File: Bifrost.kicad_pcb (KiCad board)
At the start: 4 copper layers, 68.6 x 53.3 mm, 109 parts, among them IC1 DS1085Z-10+, IC2 DS1085Z-10+, J1 OIP, J10 Barrel_Jack_Switch, J5 CalCK, U1 HMC900LP5E, U2 HMC860LP3E, U5 74AHC1G04, U6 74AHC1G04

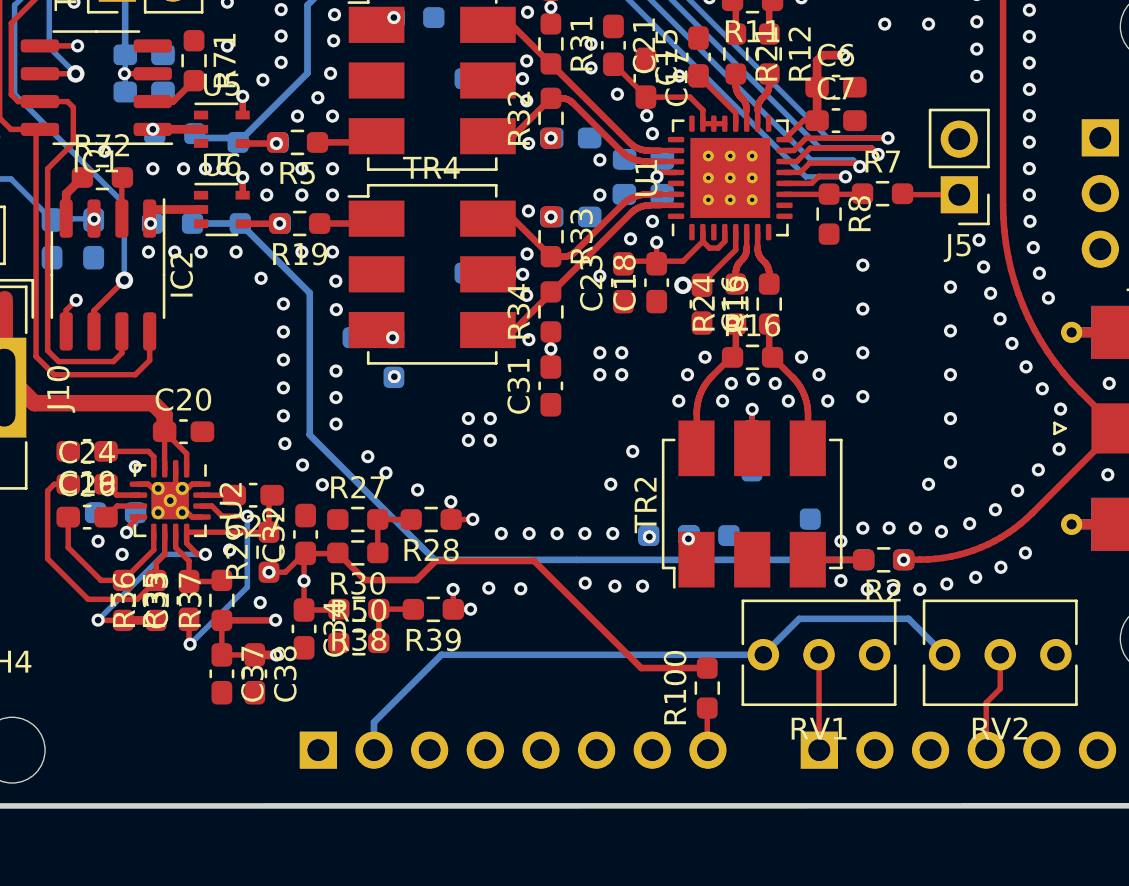
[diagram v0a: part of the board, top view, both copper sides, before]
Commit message: Added capacitors on potars
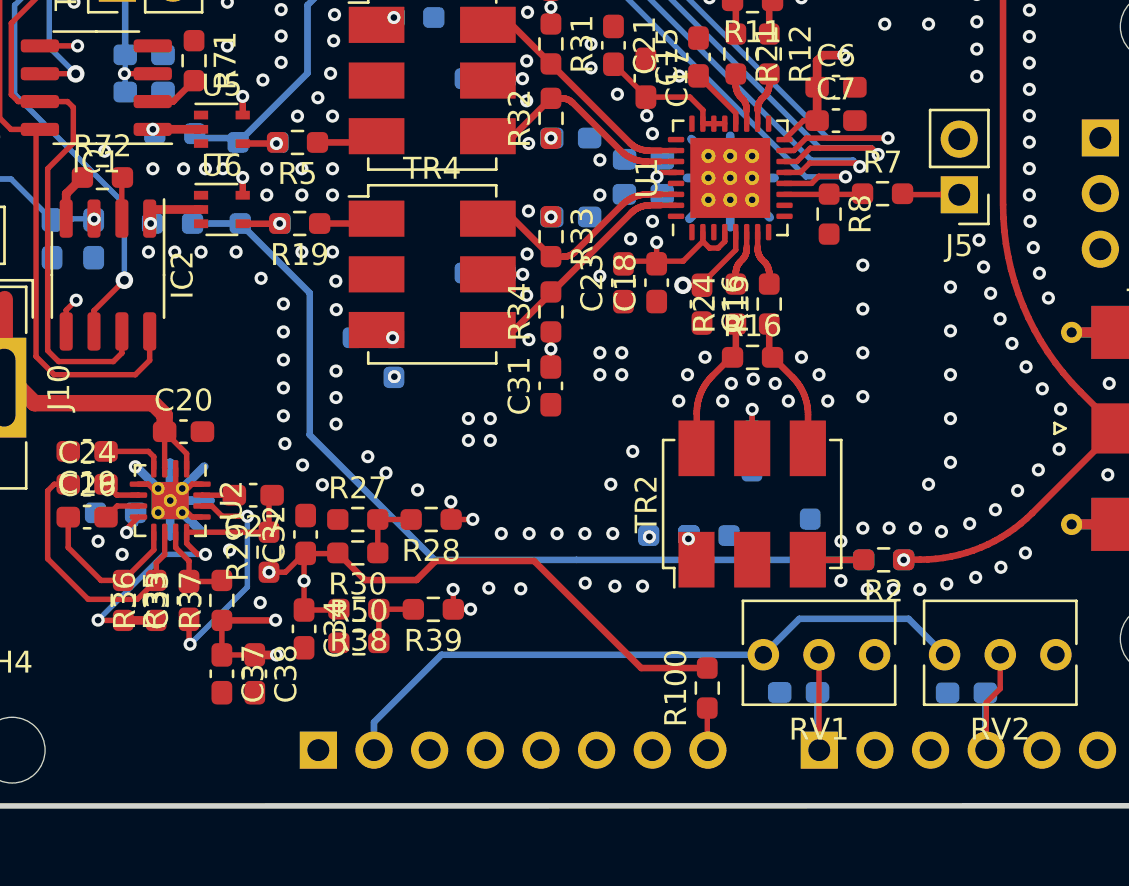
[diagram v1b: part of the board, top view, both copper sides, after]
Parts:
- added C5: 100n, Capacitor_SMD:C_0603_1608Metric_Pad1.08x0.95mm_HandSolder, B.Cu at (164.1, 126.5)
- added C8: 100n, Capacitor_SMD:C_0603_1608Metric_Pad1.08x0.95mm_HandSolder, B.Cu at (171.7, 126.5)
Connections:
- AD1 pad 2: (no net) -> /AD1
- AD1 pad 3: (no net) -> /AD2
- AD1 pad 5: (no net) -> /AD4
- AD1 pad 6: (no net) -> /AD5
- ICSP1 pad 1: (no net) -> /MISO2
- ICSP1 pad 2: (no net) -> /+5V_Adr_3
- ICSP1 pad 3: (no net) -> /SCK2
- ICSP1 pad 4: (no net) -> /MOSI2
- ICSP1 pad 5: (no net) -> /RESET2
- ICSP2 pad 1: (no net) -> /MISO_0
- ICSP2 pad 2: (no net) -> /+5V_Ard_0
- ICSP2 pad 3: (no net) -> /SCK_0
- ICSP2 pad 4: (no net) -> /MOSI_0
- ICSP2 pad 5: (no net) -> /RESET_0
- IOH1 pad 1: (no net) -> /IO8
- IOH1 pad 2: (no net) -> /IO9
- IOH1 pad 8: (no net) -> /AREF
- IOL1 pad 1: (no net) -> /IO0
- IOL1 pad 2: (no net) -> /IO1
- IOL1 pad 3: (no net) -> /IO2
- IOL1 pad 4: (no net) -> /IO3
- IOL1 pad 5: (no net) -> /IO4
- IOL1 pad 6: (no net) -> /IO5
- POWER1 pad 1: (no net) -> Net-(POWER1-Pad1)
- POWER1 pad 3: (no net) -> /RESET
- POWER1 pad 4: (no net) -> /+3V3
- POWER1 pad 5: (no net) -> /+5V_Ard_1
- TR1 pad 2: (no net) -> Net-(TR1-Pad2)
- TR2 pad 2: (no net) -> Net-(TR2-Pad2)
- TR3 pad 2: (no net) -> Net-(TR3-Pad2)
- TR4 pad 2: (no net) -> Net-(TR4-Pad2)
- U1 pad 1: (no net) -> Net-(U1-Pad1)
- U1 pad 10: (no net) -> Net-(U1-Pad10)
- U1 pad 17: (no net) -> Net-(U1-Pad17)
- U1 pad 24: (no net) -> Net-(U1-Pad24)
- U1 pad 25: (no net) -> Net-(U1-Pad25)
- U1 pad 29: (no net) -> Net-(U1-Pad29)
- U1 pad 3: (no net) -> Net-(U1-Pad3)
- U1 pad 32: (no net) -> Net-(U1-Pad32)
- U1 pad 8: (no net) -> Net-(U1-Pad8)
- U1 pad 9: (no net) -> Net-(U1-Pad9)
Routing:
- net GND: track 8.77 -> 42.4 mm
- net /AD0: track 4.36 -> 7.02 mm
- net /AD3: track 4.62 -> 7.25 mm

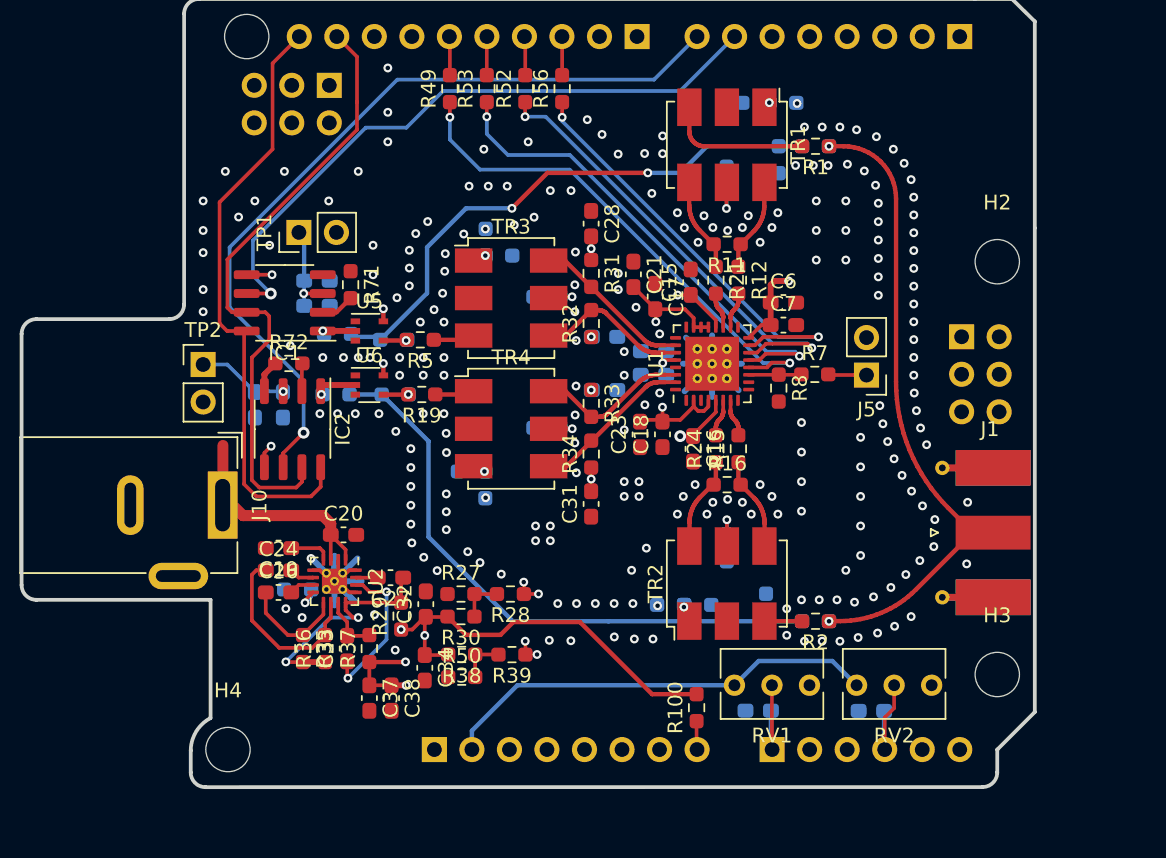
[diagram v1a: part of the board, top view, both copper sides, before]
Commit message: Rearranged the serigraphs
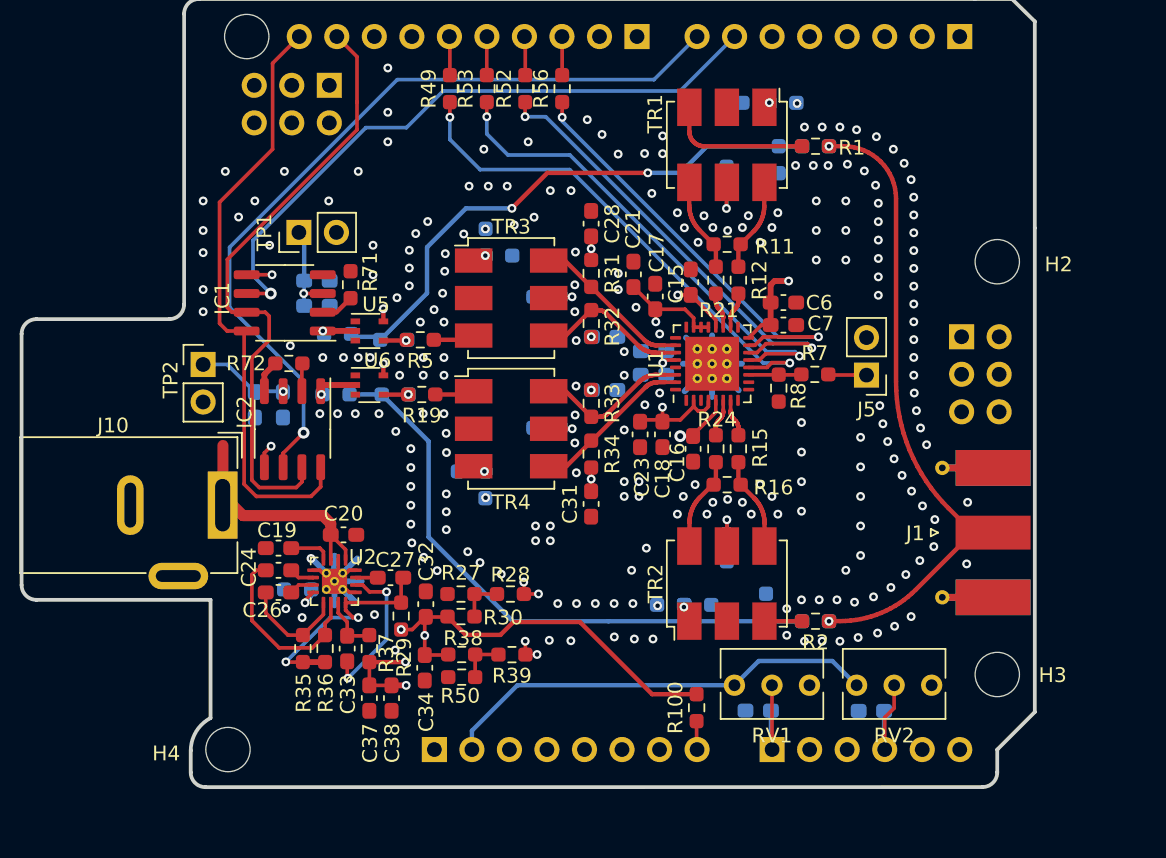
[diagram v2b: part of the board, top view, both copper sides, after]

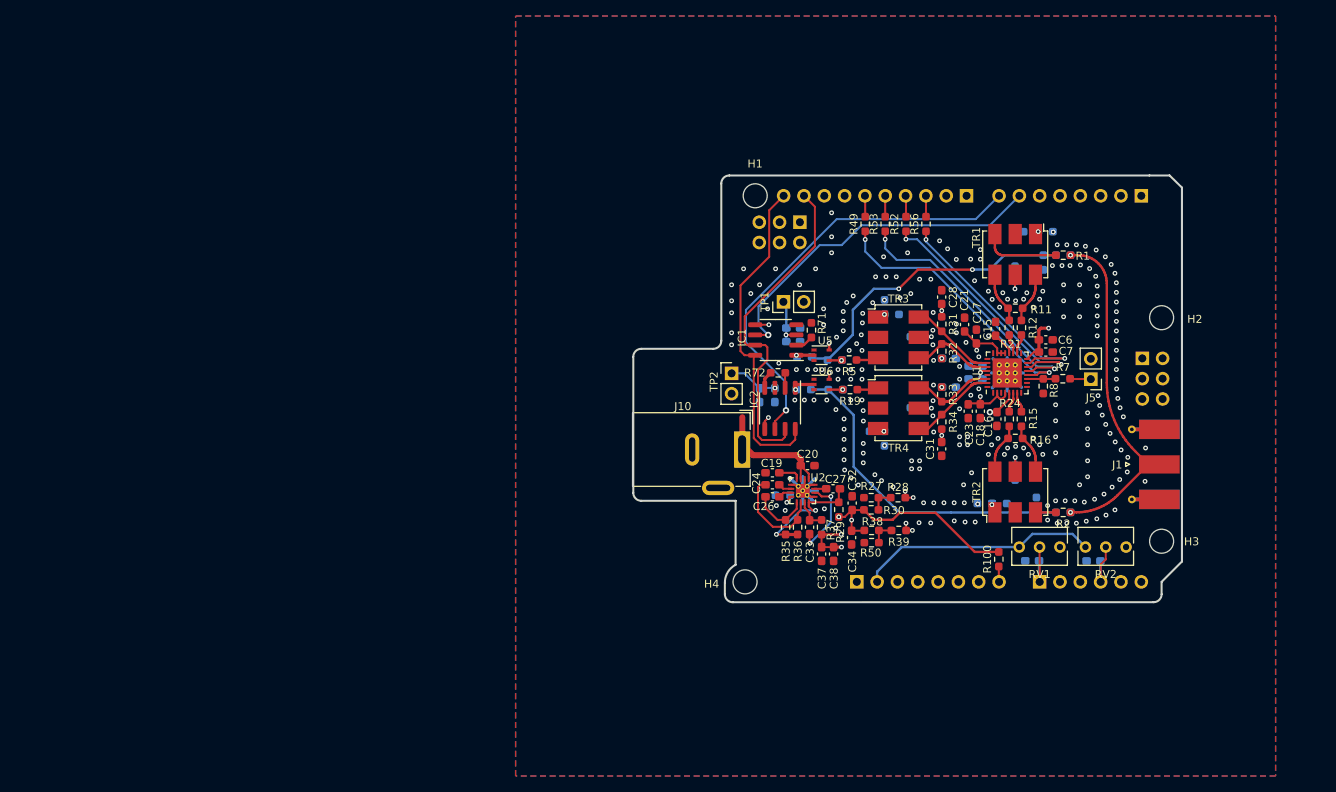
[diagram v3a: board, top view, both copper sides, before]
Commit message: Added fixed gain amplifiers Tweaked the filtering of AVDD & DVDD Began placing componants Put in feuille hierarchique
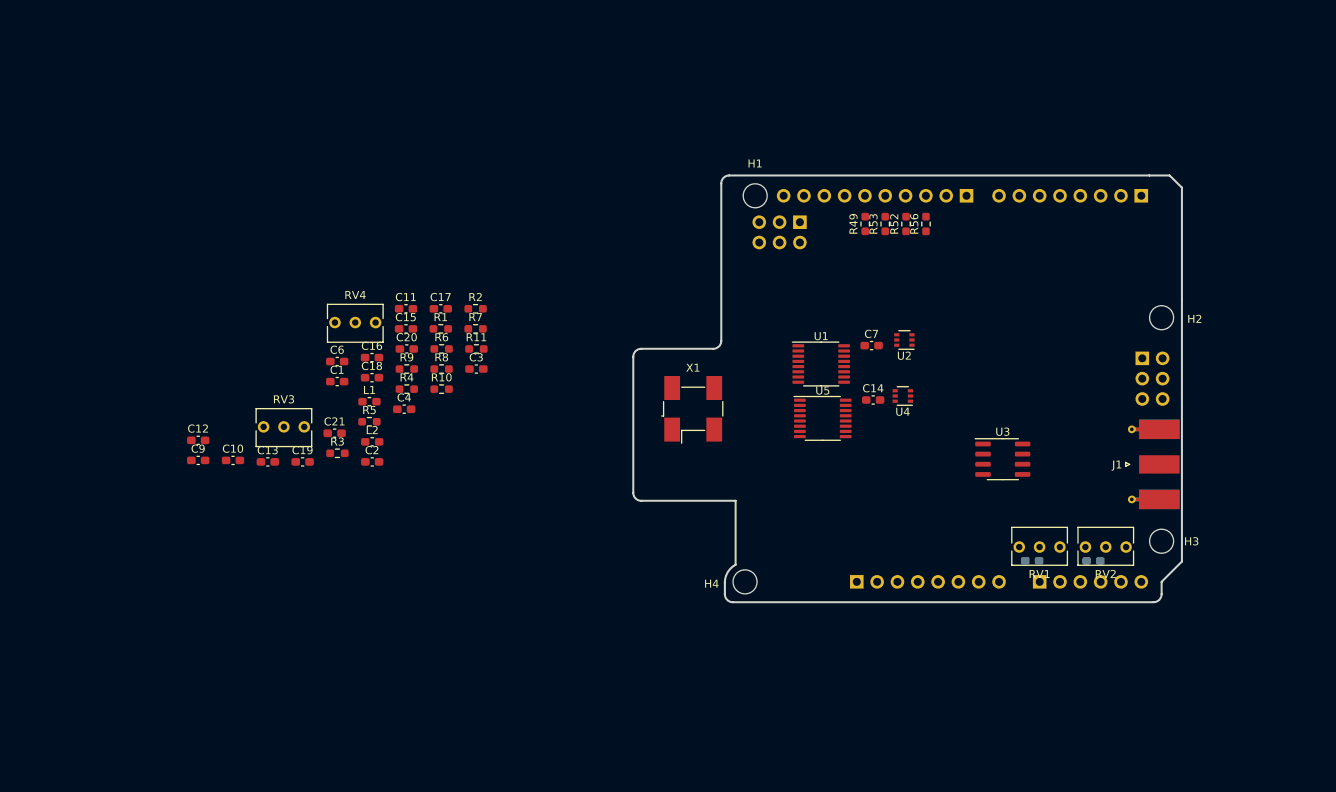
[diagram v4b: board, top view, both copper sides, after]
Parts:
- removed C22, C28, C29, C30, C31: 100p, Capacitor_SMD:C_0603_1608Metric_Pad1.08x0.95mm_HandSolder
- removed C23, C24, C25, C26, C27, C33, C34, C37: 100n, Capacitor_SMD:C_0603_1608Metric_Pad1.08x0.95mm_HandSolder
- removed C32, C38, C43, C44: 10u, Capacitor_SMD:C_0603_1608Metric_Pad1.08x0.95mm_HandSolder
- removed C45, C46: 10µ, Capacitor_SMD:C_0603_1608Metric_Pad1.08x0.95mm_HandSolder
- removed IC1, IC2: DS1085Z-10+, Package_SO:SO-8_3.9x4.9mm_P1.27mm
- removed J10: Barrel_Jack_Switch, LibPersoNadj:BarrelJack_Swc
- removed J5: CalCK, Connector_PinHeader_2.54mm:PinHeader_1x02_P2.54mm_Vertical
- removed R100, R14, R17, R18, R19, R20, R22, R23, R25, R26, R28, R40, R41, R42: 0, Resistor_SMD:R_0603_1608Metric_Pad0.98x0.95mm_HandSolder
- removed R12, R15, R21, R24: 174, Resistor_SMD:R_0603_1608Metric_Pad0.98x0.95mm_HandSolder
- removed R13, R71, R72: 510, Resistor_SMD:R_0603_1608Metric_Pad0.98x0.95mm_HandSolder
- removed R16: 140, Resistor_SMD:R_0603_1608Metric_Pad0.98x0.95mm_HandSolder
- removed R27, R30, R38, R50: 1k, Resistor_SMD:R_0603_1608Metric_Pad0.98x0.95mm_HandSolder
- removed R29, R37: 0.2, Resistor_SMD:R_0603_1608Metric_Pad0.98x0.95mm_HandSolder
- removed R31, R32, R33, R34: 51, Resistor_SMD:R_0603_1608Metric_Pad0.98x0.95mm_HandSolder
- removed R35, R36: 1, Resistor_SMD:R_0603_1608Metric_Pad0.98x0.95mm_HandSolder
- removed R39: DEPOP, Resistor_SMD:R_0603_1608Metric_Pad0.98x0.95mm_HandSolder
- removed TP1, TP2: TestPoint_2Pole, Connector_PinHeader_2.54mm:PinHeader_1x02_P2.54mm_Vertical
- removed TR1, TR2, TR3, TR4: ADT2-1T, RF_Mini-Circuits:Mini-Circuits_CD542_H2.84mm
- removed U6: 74AHC1G04, Package_TO_SOT_SMD:SOT-353_SC-70-5
- added C10: 53n, Capacitor_SMD:C_0603_1608Metric_Pad1.08x0.95mm_HandSolder, F.Cu at (64.2, 114.0)
- added C11: 100n, Capacitor_SMD:C_0603_1608Metric_Pad1.08x0.95mm_HandSolder, F.Cu at (85.8, 95.0)
- added C12: 100n, Capacitor_SMD:C_0603_1608Metric_Pad1.08x0.95mm_HandSolder, F.Cu at (59.8, 111.4)
- added C13: 10n, Capacitor_SMD:C_0603_1608Metric_Pad1.08x0.95mm_HandSolder, F.Cu at (68.5, 114.1)
- added C14: 53n, Capacitor_SMD:C_0603_1608Metric_Pad1.08x0.95mm_HandSolder, F.Cu at (144.2, 106.4)
- added C9: 1u, Capacitor_SMD:C_0603_1608Metric_Pad1.08x0.95mm_HandSolder, F.Cu at (59.8, 114.0)
- added L1: 10u, Inductor_SMD:L_0603_1608Metric_Pad1.05x0.95mm_HandSolder, F.Cu at (81.2, 106.6)
- added L2: 10u, Inductor_SMD:L_0603_1608Metric_Pad1.05x0.95mm_HandSolder, F.Cu at (81.6, 111.6)
- added RV3: POT, Potentiometer_THT:Potentiometer_Bourns_3266Y_Vertical, F.Cu at (73.1, 109.8)
- added RV4: POT, Potentiometer_THT:Potentiometer_Bourns_3266Y_Vertical, F.Cu at (82.0, 96.7)
- added U3: AD8000, Package_SO:SOIC-8_3.9x4.9mm_P1.27mm, F.Cu at (160.4, 113.8)
- added U4: BGA2851, Package_TO_SOT_SMD:SOT-363_SC-70-6, F.Cu at (147.9, 105.9)
- added X1: SPXO-50M, Oscillator:Oscillator_SMD_SeikoEpson_SG8002CA-4Pin_7.0x5.0mm_HandSoldering, F.Cu at (121.7, 107.5)
- C1: value 100n -> 10n; moved to F.Cu
- C15: value 100n -> 53n
- C17: value 100p -> 100n
- C18: value 100p -> 10u
- C19: value 1u -> 10u
- C2, C4: value 100p -> 100n; moved to F.Cu
- C20: value 4.7u -> 10u
- C21: value 100n -> 10u
- C3: moved to F.Cu
- C7: value 100p -> 53n
- R1: value 510 -> 15k
- R10: value 0 -> 2; moved to F.Cu
- R11: value 140 -> 2
- R2: value 510 -> 5k
- R3: value 0 -> 5k; moved to F.Cu
- R4, R9: value 0 -> 1k; moved to F.Cu
- R49, R52, R53, R56: value 510 -> 300
- R5, R7: value 0 -> 1k
- R6: value 510 -> 1k; moved to F.Cu
- R8: value 51 -> 1k
- U1: value HMC900LP5E -> AD5932; footprint Package_DFN_QFN:QFN-32-1EP_5x5mm_P0.5mm_EP3.65x3.65mm_ThermalVias -> Package_SO:TSSOP-16_4.4x5mm_P0.65mm
- U2: value HMC860LP3E -> BGA2851; footprint Package_DFN_QFN:QFN-16-1EP_3x3mm_P0.5mm_EP1.7x1.7mm_ThermalVias -> Package_TO_SOT_SMD:SOT-363_SC-70-6
- U5: value 74AHC1G04 -> AD5932; footprint Package_TO_SOT_SMD:SOT-353_SC-70-5 -> Package_SO:TSSOP-16_4.4x5mm_P0.65mm
- moved C6 88.6 mm to (77.2, 101.6)
- moved R9 80.7 mm to (85.9, 102.5), turned to 0 degrees
- moved C21 79.9 mm to (76.9, 110.5), turned to 0 degrees
- moved R6 78.6 mm to (90.2, 100.0)
- moved C16 78.5 mm to (81.5, 101.1), turned to 0 degrees
- moved R1 78.3 mm to (90.2, 97.5), turned to 0 degrees
- moved R2 77.7 mm to (94.5, 95.0), turned to 0 degrees
- moved C18 76.2 mm to (81.5, 103.6), turned to 0 degrees
- moved R10 75.7 mm to (90.2, 105.0), turned to 0 degrees
- moved R8 75.2 mm to (90.2, 102.5), turned to 0 degrees
- moved C15 73.7 mm to (85.8, 97.5), turned to 0 degrees
- moved R7 73.7 mm to (94.5, 97.5)
- moved R11 67.6 mm to (94.6, 100.0), turned to 0 degrees
- moved C17 67.0 mm to (90.2, 95.0), turned to 0 degrees
- moved R5 60.5 mm to (81.2, 109.1), turned to 0 degrees
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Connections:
- AD1 pad 2: /AD1 -> (no net)
- AD1 pad 3: /AD2 -> (no net)
- AD1 pad 5: /AD4 -> (no net)
- AD1 pad 6: /AD5 -> (no net)
- C1 pad 1: GND -> Net-(C1-Pad1)
- C1 pad 2: Net-(C1-Pad2) -> VDDA
- C15 pad 1: CMO -> Net-(C15-Pad1)
- C15 pad 2: GND -> Net-(C15-Pad2)
- C16 pad 1: CMO -> Net-(C16-Pad1)
- C17 pad 1: GND -> VDD
- C17 pad 2: VDDA -> GND
- C18 pad 2: VDDA -> /+5V_Ard_0
- C19 pad 1: Net-(C19-Pad1) -> GND
- C19 pad 2: GND -> VDD
- C2 pad 1: GND -> VDDA
- C2 pad 2: Net-(C1-Pad2) -> GND
- C20 pad 1: /Sheet6188E6DC/5.5V -> GND
- C20 pad 2: GND -> /+5V_Ard_0
- C3 pad 1: GND -> VDD
- C3 pad 2: Net-(C3-Pad2) -> GND
- C4 pad 1: GND -> Net-(C4-Pad1)
- C4 pad 2: Net-(C3-Pad2) -> GND
- C6 pad 1: VCC -> VDDA
- C7 pad 1: VCC -> Net-(C7-Pad1)
- C7 pad 2: GND -> Net-(C7-Pad2)
- ICSP1 pad 1: /MISO2 -> (no net)
- ICSP1 pad 2: /+5V_Adr_3 -> (no net)
- ICSP1 pad 3: /SCK2 -> (no net)
- ICSP1 pad 4: /MOSI2 -> (no net)
- ICSP1 pad 5: /RESET2 -> (no net)
- ICSP2 pad 1: /MISO_0 -> (no net)
- ICSP2 pad 3: /SCK_0 -> (no net)
- ICSP2 pad 4: /MOSI_0 -> (no net)
- ICSP2 pad 5: /RESET_0 -> (no net)
- IOH1 pad 1: /IO8 -> (no net)
- IOH1 pad 10: /SCL -> (no net)
- IOH1 pad 2: /IO9 -> (no net)
- IOH1 pad 8: /AREF -> (no net)
- IOH1 pad 9: /SDA -> (no net)
- IOL1 pad 1: /IO0 -> (no net)
- IOL1 pad 2: /IO1 -> (no net)
- J1 pad 1: Net-(J1-Pad1) -> Net-(C9-Pad2)
- POWER1 pad 1: Net-(POWER1-Pad1) -> (no net)
- POWER1 pad 3: /RESET -> (no net)
- POWER1 pad 4: /+3V3 -> (no net)
- POWER1 pad 5: /+5V_Ard_1 -> (no net)
- POWER1 pad 8: /VIN -> (no net)
- R1 pad 1: Net-(J1-Pad1) -> Net-(C9-Pad1)
- R1 pad 2: /Sheet60D21B6D/OutI+ -> Net-(R1-Pad2)
- R10 pad 1: Net-(R10-Pad1) -> VDD
- R10 pad 2: GND -> Net-(L1-Pad2)
- R11 pad 1: Net-(R11-Pad1) -> VDDA
- R2 pad 1: Net-(J1-Pad1) -> Net-(R2-Pad1)
- R2 pad 2: /Sheet60D21B6D/OutQ+ -> Net-(C10-Pad2)
- R3 pad 2: Net-(IC1-Pad1) -> Net-(C15-Pad2)
- R4 pad 1: Net-(R3-Pad1) -> +2V5
- R4 pad 2: Net-(R4-Pad2) -> VDDA
- R5 pad 1: /Sheet60D21B6D/InI+ -> +2V5
- R5 pad 2: Net-(R4-Pad2) -> GND
- R53 pad 1: /SDO_S -> (no net)
- R6 pad 1: Net-(R3-Pad1) -> VDDA
- R6 pad 2: Net-(J1-Pad1) -> Net-(C10-Pad2)
- R7 pad 1: Net-(R7-Pad1) -> Net-(C10-Pad2)
- R7 pad 2: /Sheet60D21B6D/CalCK -> GND
- R8 pad 1: Net-(R7-Pad1) -> VDDA
- R8 pad 2: GND -> Net-(C15-Pad2)
- R9 pad 1: Net-(R3-Pad1) -> Net-(C15-Pad2)
- U1 pad 1: Net-(U1-Pad1) -> Net-(C1-Pad1)
- U1 pad 10: Net-(U1-Pad10) -> /IO3
- U1 pad 11: Net-(R7-Pad1) -> /SDI_S
- U1 pad 13: /SDO_S -> /SEN_S
- U1 pad 14: /SDI_S -> /IO4
- U1 pad 15: /SEN_S -> GND
- U1 pad 16: VCC -> Net-(C7-Pad1)
- U1 pad 3: Net-(U1-Pad3) -> VDD
- U1 pad 4: VDDA -> Net-(C4-Pad1)
- U1 pad 5: CMO -> GND
- U1 pad 6: /Sheet60D21B6D/sheet60F5ADAC/S- -> Net-(U1-Pad6)
- U1 pad 7: /Sheet60D21B6D/sheet60F5ADAC/S+ -> (no net)
- U1 pad 8: Net-(U1-Pad8) -> (no net)
- U1 pad 9: Net-(U1-Pad9) -> /IO2
- U2 pad 1: /Sheet6188E6DC/5.5V -> VDDA
- U2 pad 3: /Sheet6188E6DC/5.5V -> Net-(C10-Pad1)
- U2 pad 4: Net-(C19-Pad1) -> GND
- U2 pad 6: Net-(C24-Pad2) -> Net-(C7-Pad2)
- U5 pad 1: (no net) -> Net-(C13-Pad1)
- U5 pad 2: Net-(IC1-Pad1) -> VDDA
- U5 pad 3: GND -> VDD
- U5 pad 4: Net-(R4-Pad2) -> Net-(C16-Pad1)
- U5 pad 5: VCC -> GND
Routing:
- net VCC: track 65.3 -> 0.00 mm, vias 5 -> 0
- net /IO7: track 55.1 -> 0.00 mm, vias 1 -> 0
- net VDDA: track 47.7 -> 0.00 mm, vias 16 -> 0
- net Net-(J1-Pad1): track 46.2 -> 0.00 mm, vias 2 -> 0
- net /IO6: track 44.0 -> 0.00 mm, vias 1 -> 0
- net GND: track 42.4 -> 0.00 mm, vias 207 -> 0
- net /SDA: track 41.9 -> 0.00 mm
- net /SCL: track 41.3 -> 0.00 mm
- net Net-(R10-Pad1): track 40.8 -> 0.00 mm
- net Net-(R3-Pad1): track 37.8 -> 0.00 mm, vias 2 -> 0
- net /SCK_S: track 34.7 -> 0.00 mm, vias 2 -> 0
- net /SDO_S: track 33.2 -> 0.00 mm, vias 2 -> 0
- net /SDI_S: track 31.5 -> 0.00 mm, vias 2 -> 0
- net /+5V_Ard_2: track 29.9 -> 0.00 mm
- net /SEN_S: track 29.6 -> 0.00 mm, vias 2 -> 0
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- removed copper zone on In2.Cu, net CMI
- removed copper zone on In2.Cu, net CMO
- removed copper zone on B.Cu, net GND
- removed copper zone on F.Cu, net GND
- removed copper zone on In1.Cu, net GND
- removed copper zone on In2.Cu, net GND
- removed copper zone on In2.Cu, net VCC
- removed copper zone on In2.Cu, net VDDA
